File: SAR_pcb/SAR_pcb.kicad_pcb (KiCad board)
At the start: 4 copper layers, 67.6 x 49.5 mm, 32 parts, among them J1 Conn_Coaxial_Power, J10 Conn_Coaxial, J2 Conn_Coaxial_Power, J3 Conn_02x10_Top_Bottom, J4 Conn_01x06, J9 Conn_Coaxial, SW1 SW_Push, U2 10B_SAR

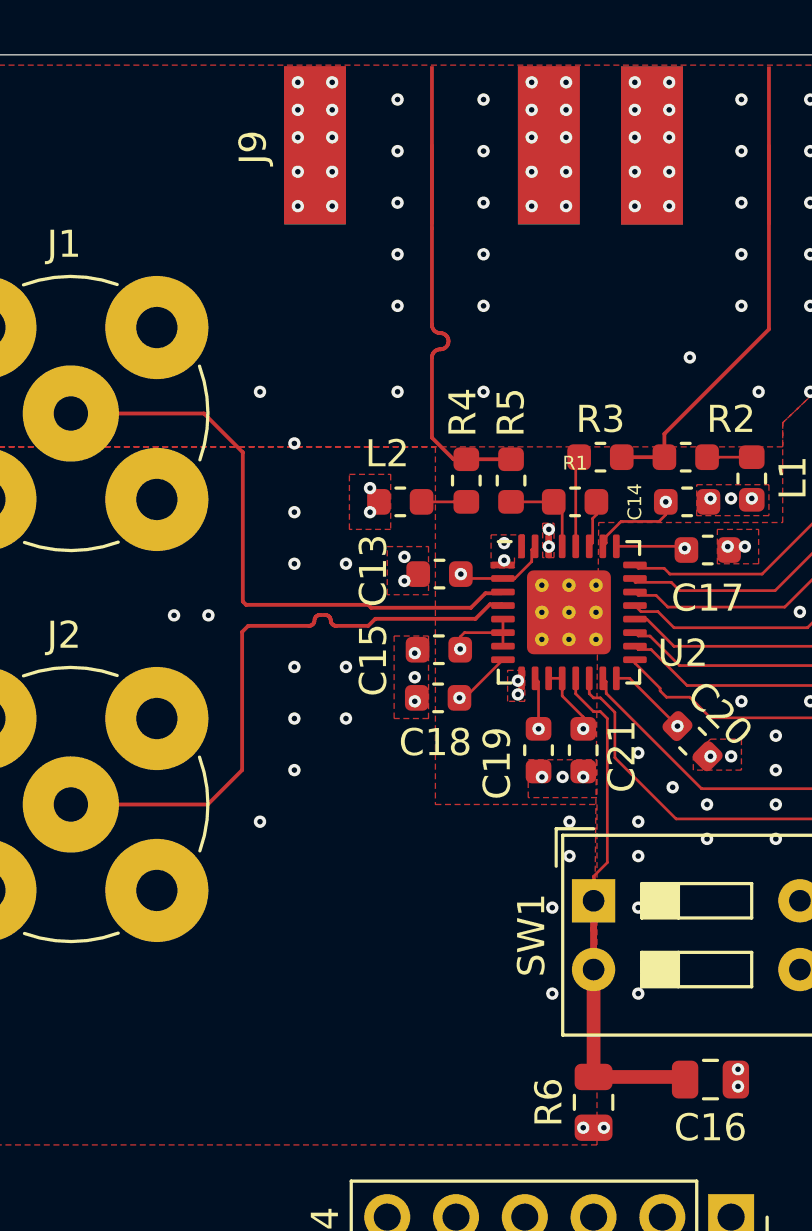
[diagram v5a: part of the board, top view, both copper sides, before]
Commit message: Added input termination
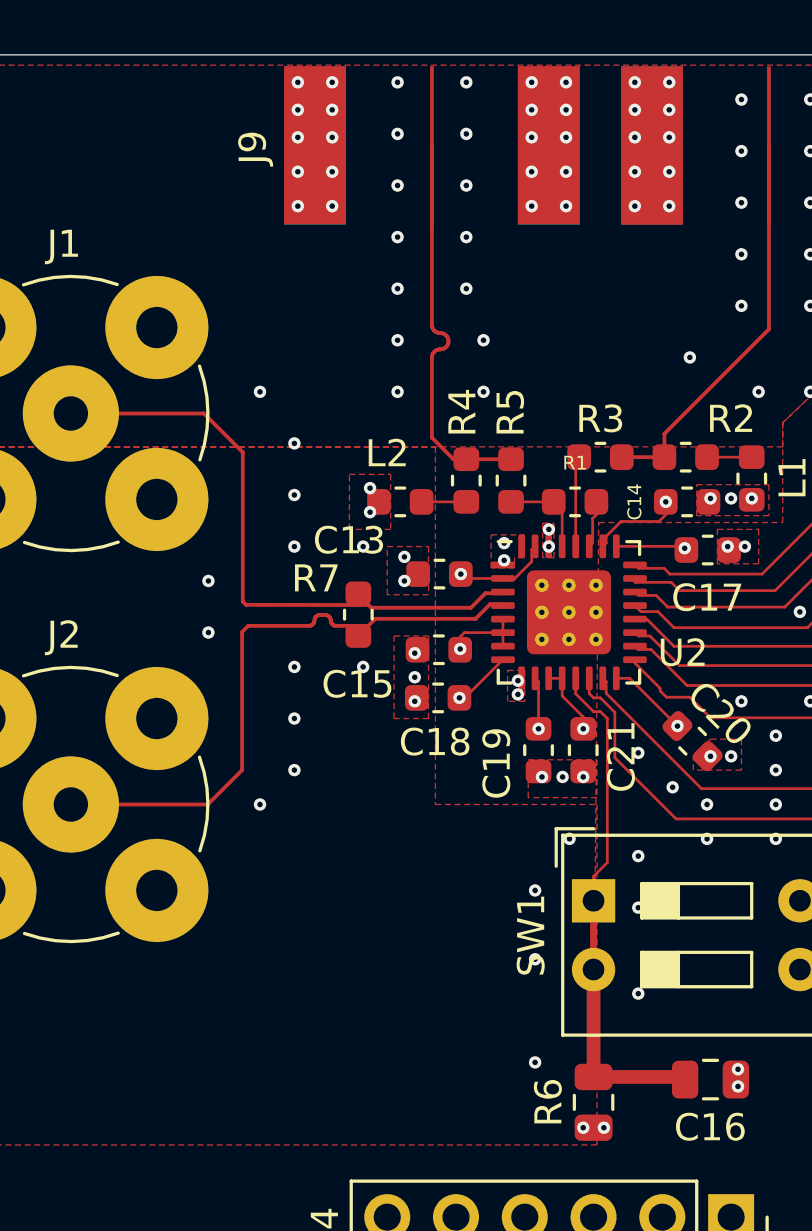
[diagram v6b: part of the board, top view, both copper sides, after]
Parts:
- added R7: 100, Resistor_SMD:R_0603_1608Metric, F.Cu at (141.4, 93.3)
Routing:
- net GND: vias 128 -> 158
- net (no net): vias 30 -> 0
- removed copper zone on F.Cu, net (none)
